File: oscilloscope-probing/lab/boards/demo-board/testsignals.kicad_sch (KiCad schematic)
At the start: 1 part, among them U4 XC7A35T-2FGG484I

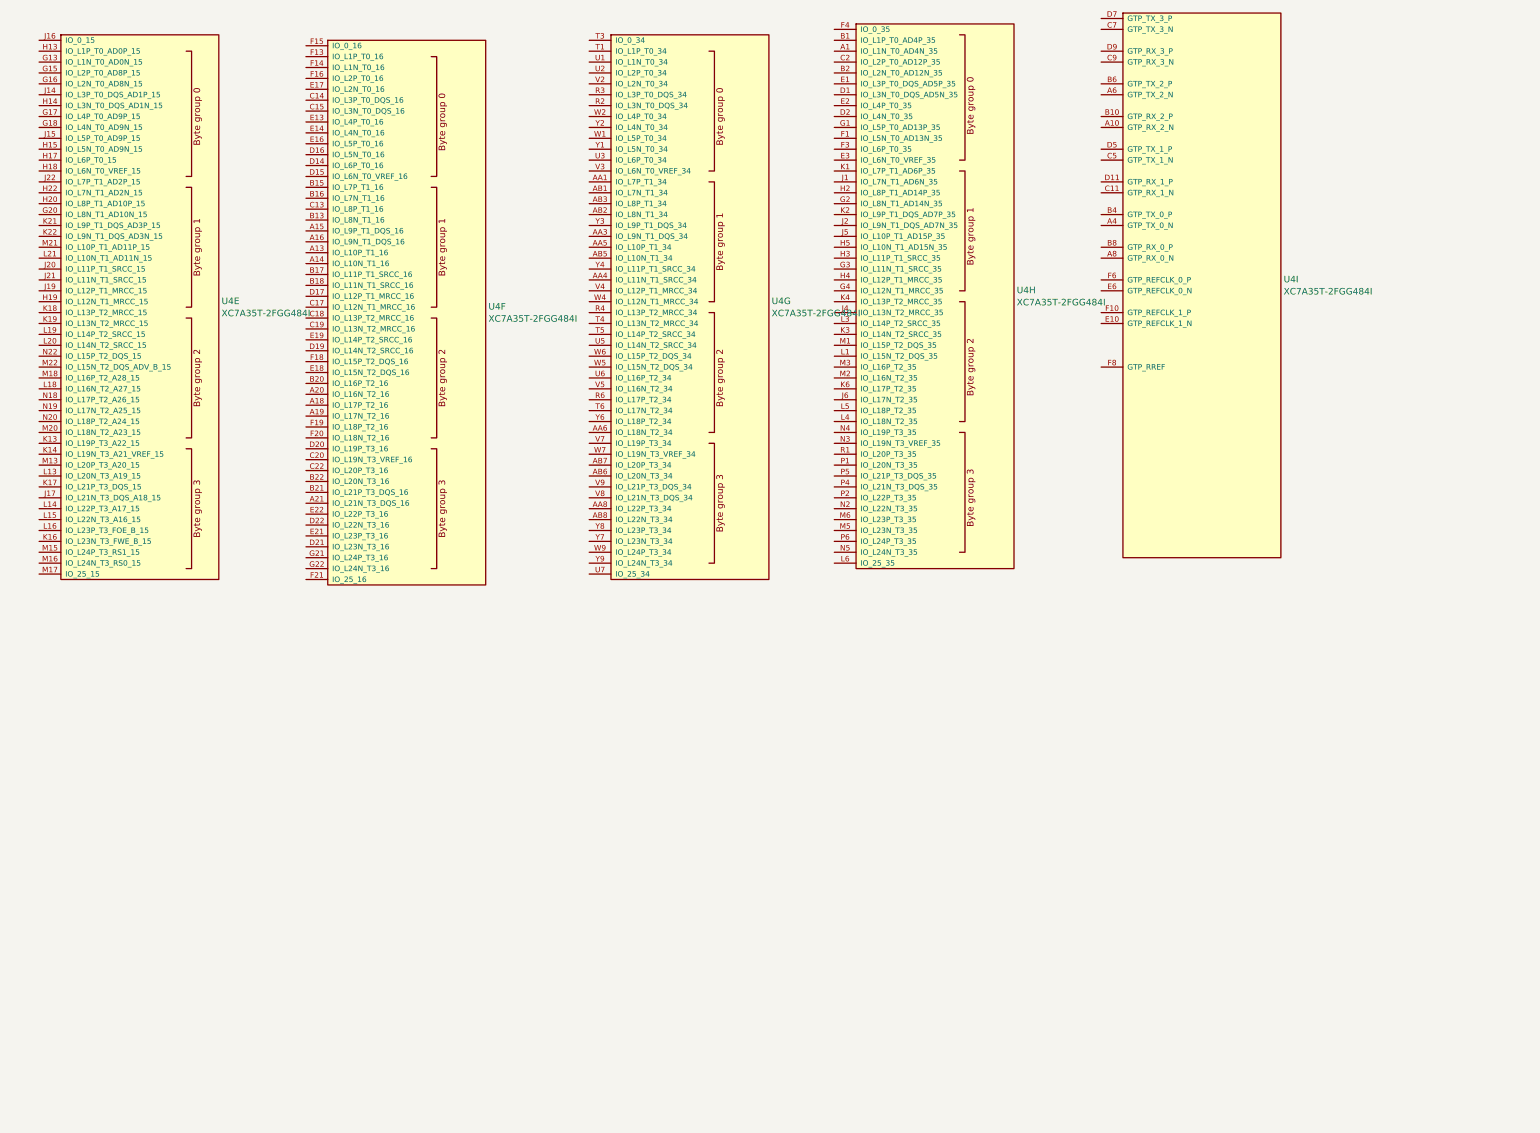
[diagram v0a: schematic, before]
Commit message: Finished initial demo board schematic
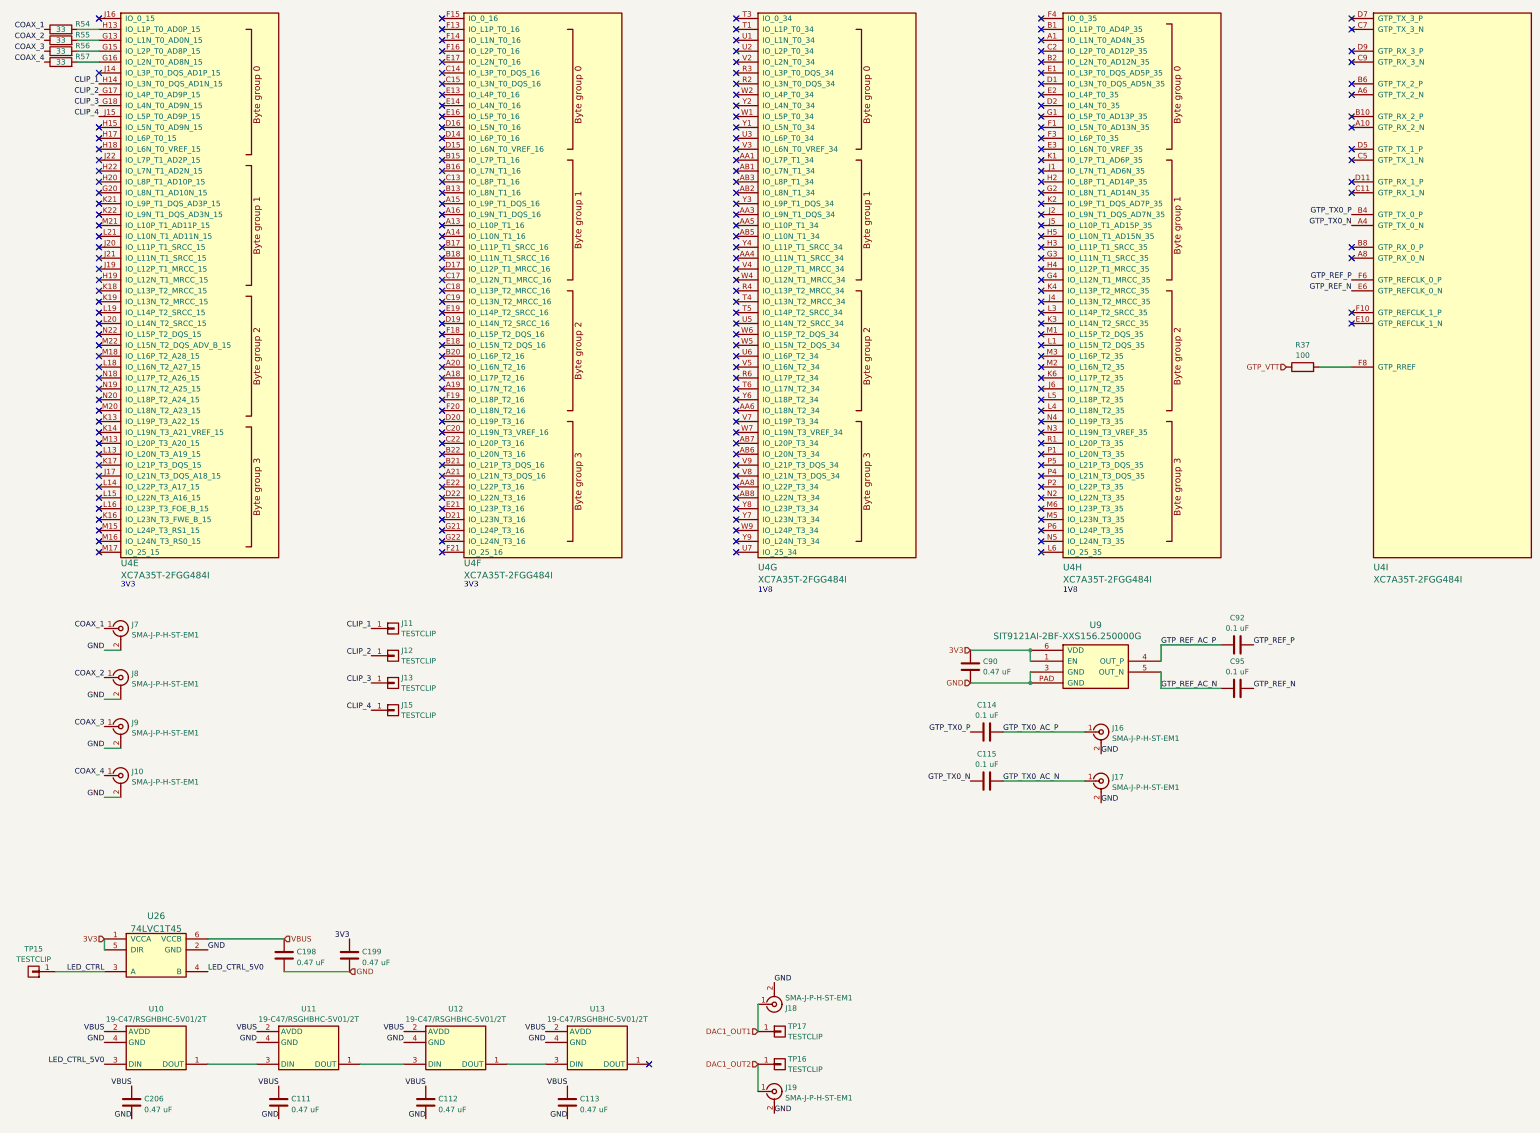
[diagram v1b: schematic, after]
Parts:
- added C111, C112, C113, C198, C199, C206, C90: 0.47 uF, azonenberg_pcb:EIA_0402_CAP_NOSILK, symbol device:C
- added C114, C115, C92, C95: 0.1 uF, azonenberg_pcb:EIA_0402_CAP_NOSILK, symbol device:C
- added J10, J16, J17, J18, J19, J7, J8, J9: SMA-J-P-H-ST-EM1, symbol conn:CONN_COAXIAL
- added J11, J12, J13, J15, TP15, TP16, TP17: TESTCLIP, symbol conn:CONN_01X01
- added R37: 100, azonenberg_pcb:EIA_0402_RES_NOSILK, symbol device:R
- added R54, R55, R56, R57: 33, symbol device:R
- added U10, U11, U12, U13: 19-C47/RSGHBHC-5V01/2T, symbol special-azonenberg:19-C47_RSGHBHC-5V01_2T
- added U26: 74LVC1T45, azonenberg_pcb:DFN_6_0.5MM_1.6x1.6MM_TI_DPK, symbol special-azonenberg:74AVC1T45
- added U9: SIT9121AI-2BF-XXS156.250000G, azonenberg_pcb:OSCILLATOR_LVDS_3.2x2.5, symbol osc-azonenberg:OSC_LVDS
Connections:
- net GTP_TX0_N: now reaches U4.A4 (GTP_TX_0_N)
- net GTP_TX0_N: now also C115.1
- net GTP_TX0_P: now reaches U4.B4 (GTP_TX_0_P)
- net GTP_TX0_P: now also C114.1
- net GTP_REF_N: now reaches U4.E6 (GTP_REFCLK_0_N)
- net GTP_REF_N: now also C95.2
- net GTP_REF_P: now reaches U4.F6 (GTP_REFCLK_0_P)
- net GTP_REF_P: now also C92.2
- net at U4.F8 (GTP_RREF): now also R37.2
- net at U4.G13 (IO_L1N_T0_AD0N_15): now also R55.2
- net at U4.G15 (IO_L2P_T0_AD8P_15): now also R56.2
- net at U4.G16 (IO_L2N_T0_AD8N_15): now also R57.2
- net CLIP_2: now reaches U4.G17 (IO_L4P_T0_AD9P_15)
- net CLIP_2: now also J12.1 (P1)
- net CLIP_3: now reaches U4.G18 (IO_L4N_T0_AD9N_15)
- net CLIP_3: now also J13.1 (P1)
- net at U4.H13 (IO_L1P_T0_AD0P_15): now also R54.2
- net CLIP_1: now reaches U4.H14 (IO_L3N_T0_DQS_AD1N_15)
- net CLIP_1: now also J11.1 (P1)
- net CLIP_4: now reaches U4.J15 (IO_L5P_T0_AD9P_15)
- net CLIP_4: now also J15.1 (P1)
- new net: U11.1 (DOUT), U12.3 (DIN)
- new net: U10.1 (DOUT), U11.3 (DIN)
- new net: U12.1 (DOUT), U13.3 (DIN)
- new net 3V3: C199.1, C90.1, U26.1 (VCCA), U26.5 (DIR), U9.1 (EN), U9.6 (VDD)
- new net COAX_1: J7.1 (In), R54.1
- new net COAX_2: J8.1 (In), R55.1
- new net COAX_3: J9.1 (In), R56.1
- new net COAX_4: J10.1 (In), R57.1
- new net DAC1_OUT1: J18.1 (In), TP17.1 (P1)
- new net DAC1_OUT2: J19.1 (In), TP16.1 (P1)
- new net GND: C111.2, C112.2, C113.2, C198.2, C199.2, C206.2, C90.2, J10.2 (Ext), J16.2 (Ext), J17.2 (Ext), J18.2 (Ext), J19.2 (Ext), J7.2 (Ext), J8.2 (Ext), J9.2 (Ext), U10.4 (GND), U11.4 (GND), U12.4 (GND), U13.4 (GND), U26.2 (GND), U9.3 (GND), U9.PAD (GND)
- new net GTP_REF_AC_N: C95.1, U9.5 (OUT_N)
- new net GTP_REF_AC_P: C92.1, U9.4 (OUT_P)
- new net GTP_TX0_AC_N: C115.2, J17.1 (In)
- new net GTP_TX0_AC_P: C114.2, J16.1 (In)
- new net GTP_VTT: R37.1
- new net LED_CTRL: TP15.1 (P1), U26.3 (A)
- new net LED_CTRL_5V0: U10.3 (DIN), U26.4 (B)
- new net VBUS: C111.1, C112.1, C113.1, C198.1, C206.1, U10.2 (AVDD), U11.2 (AVDD), U12.2 (AVDD), U13.2 (AVDD), U26.6 (VCCB)
- no-connect marks 0 -> 209
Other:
- note added: "1V8"
- note added: "3V3"
- moved on the sheet: U4E, U4F, U4G, U4H, U4I

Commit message: Continued initial schematic, assigned footprints
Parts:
- J10, J16, J17, J18, J19, J7, J8, J9: footprint (none) -> azonenberg_pcb:CONN_SMA_EDGE_SAMTEC_SMA_J_P_H_ST_EM1
- J11, J12, J13, J15, TP15, TP16, TP17: footprint (none) -> azonenberg_pcb:TESTPOINT_SMT_KEYSTONE_5016
- R54, R55, R56, R57: footprint (none) -> azonenberg_pcb:EIA_0402_RES_NOSILK
- U10, U11, U12, U13: footprint (none) -> azonenberg_pcb:LED_EVERLIGHT_19-C47_RSGHBHC-5V01_2T
- U4: footprint (none) -> azonenberg_pcb:BGA_484_22x22_FULLARRAY_1MM
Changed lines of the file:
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@@
 			)
 		)
-		(property "Footprint" ""
+		(property "Footprint" "azonenberg_pcb:CONN_SMA_EDGE_SAMTEC_SMA_J_P_H_ST_EM1"
 			(at 276.86 198.12 0)
 			(effects
@@
 			)
 		)
-		(property "Footprint" ""
+		(property "Footprint" "azonenberg_pcb:TESTPOINT_SMT_KEYSTONE_5016"
 			(at 111.76 162.56 0)
 			(effects
@@
 			)
 		)
-		(property "Footprint" ""
+		(property "Footprint" "azonenberg_pcb:CONN_SMA_EDGE_SAMTEC_SMA_J_P_H_ST_EM1"
 			(at 48.26 173.99 0)
 			(effects
@@
 			)
 		)
-		(property "Footprint" ""
+		(property "Footprint" "azonenberg_pcb:TESTPOINT_SMT_KEYSTONE_5016"
 			(at 111.76 175.26 0)
 			(effects
@@
 			)
 		)
-		(property "Footprint" ""
+		(property "Footprint" "azonenberg_pcb:CONN_SMA_EDGE_SAMTEC_SMA_J_P_H_ST_EM1"
 			(at 48.26 162.56 0)
 			(effects
@@
 			)
 		)
-		(property "Footprint" ""
+		(property "Footprint" "azonenberg_pcb:TESTPOINT_SMT_KEYSTONE_5016"
 			(at 111.76 168.91 0)
 			(effects
@@
 			)
 		)
-		(property "Footprint" ""
+		(property "Footprint" "azonenberg_pcb:TESTPOINT_SMT_KEYSTONE_5016"
 			(at 111.76 181.61 0)
 			(effects
@@
 			)
 		)
-		(property "Footprint" ""
+		(property "Footprint" "azonenberg_pcb:TESTPOINT_SMT_KEYSTONE_5016"
 			(at 201.93 264.16 0)
 			(effects
@@
 			)
 		)
-		(property "Footprint" ""
+		(property "Footprint" "azonenberg_pcb:BGA_484_22x22_FULLARRAY_1MM"
 			(at 340.36 152.4 0)
 			(effects
@@
 					(size 1.524 1.524)
 				)
+				(hide yes)
 			)
 		)
@@
 			)
 		)
-		(property "Footprint" ""
+		(property "Footprint" "azonenberg_pcb:EIA_0402_RES_NOSILK"
 			(at 34.29 24.638 90)
 			(effects
@@
 			)
 		)
-		(property "Footprint" ""
+		(property "Footprint" "azonenberg_pcb:EIA_0402_RES_NOSILK"
 			(at 34.29 29.718 90)
 			(effects
@@
 			)
 		)
-		(property "Footprint" ""
+		(property "Footprint" "azonenberg_pcb:CONN_SMA_EDGE_SAMTEC_SMA_J_P_H_ST_EM1"
 			(at 276.86 186.69 0)
 			(effects
@@
 			)
 		)
-		(property "Footprint" ""
+		(property "Footprint" "azonenberg_pcb:TESTPOINT_SMT_KEYSTONE_5016"
 			(at 27.94 242.57 0)
 			(effects
@@
 			)
 		)
-		(property "Footprint" ""
+		(property "Footprint" "azonenberg_pcb:TESTPOINT_SMT_KEYSTONE_5016"
 			(at 201.93 256.54 0)
 			(effects
@@
 			)
 		)
-		(property "Footprint" ""
+		(property "Footprint" "azonenberg_pcb:BGA_484_22x22_FULLARRAY_1MM"
 			(at 48.26 152.4 0)
 			(effects
@@
 					(size 1.524 1.524)
 				)
+				(hide yes)
 			)
 		)
@@
 			)
 		)
-		(property "Footprint" ""
+		(property "Footprint" "azonenberg_pcb:EIA_0402_RES_NOSILK"
 			(at 34.29 27.178 90)
 			(effects
@@
 			)
 		)
-		(property "Footprint" ""
+		(property "Footprint" "azonenberg_pcb:CONN_SMA_EDGE_SAMTEC_SMA_J_P_H_ST_EM1"
 			(at 48.26 185.42 0)
 			(effects
@@
 			)
 		)
-		(property "Footprint" ""
+		(property "Footprint" "azonenberg_pcb:CONN_SMA_EDGE_SAMTEC_SMA_J_P_H_ST_EM1"
 			(at 200.66 270.51 0)
 			(effects
@@
 			)
 		)
-		(property "Footprint" ""
+		(property "Footprint" "azonenberg_pcb:CONN_SMA_EDGE_SAMTEC_SMA_J_P_H_ST_EM1"
 			(at 200.66 250.19 0)
 			(effects
@@
 			)
 		)
-		(property "Footprint" ""
+		(property "Footprint" "azonenberg_pcb:CONN_SMA_EDGE_SAMTEC_SMA_J_P_H_ST_EM1"
 			(at 48.26 196.85 0)
 			(effects
@@
 			)
 		)
-		(property "Footprint" ""
+		(property "Footprint" "azonenberg_pcb:LED_EVERLIGHT_19-C47_RSGHBHC-5V01_2T"
 			(at 85.09 265.43 0)
 			(effects
@@
 			)
 		)
-		(property "Footprint" ""
+		(property "Footprint" "azonenberg_pcb:BGA_484_22x22_FULLARRAY_1MM"
 			(at 128.27 152.4 0)
 			(effects
@@
 					(size 1.524 1.524)
 				)
+				(hide yes)
 			)
 		)
@@
 			)
 		)
-		(property "Footprint" ""
+		(property "Footprint" "azonenberg_pcb:BGA_484_22x22_FULLARRAY_1MM"
 			(at 267.97 152.4 0)
 			(effects
@@
 					(size 1.524 1.524)
 				)
+				(hide yes)
 			)
 		)
@@
 			)
 		)
-		(property "Footprint" ""
+		(property "Footprint" "azonenberg_pcb:LED_EVERLIGHT_19-C47_RSGHBHC-5V01_2T"
 			(at 119.38 265.43 0)
 			(effects
@@
 			)
 		)
-		(property "Footprint" ""
+		(property "Footprint" "azonenberg_pcb:LED_EVERLIGHT_19-C47_RSGHBHC-5V01_2T"
 			(at 49.53 265.43 0)
 			(effects
@@
 			)
 		)
-		(property "Footprint" ""
+		(property "Footprint" "azonenberg_pcb:EIA_0402_RES_NOSILK"
 			(at 34.29 32.258 90)
 			(effects
@@
 			)
 		)
-		(property "Footprint" ""
+		(property "Footprint" "azonenberg_pcb:LED_EVERLIGHT_19-C47_RSGHBHC-5V01_2T"
 			(at 152.4 265.43 0)
 			(effects
@@
 			)
 		)
-		(property "Footprint" ""
+		(property "Footprint" "azonenberg_pcb:BGA_484_22x22_FULLARRAY_1MM"
 			(at 196.85 152.4 0)
 			(effects
@@
 					(size 1.524 1.524)
 				)
+				(hide yes)
 			)
 		)

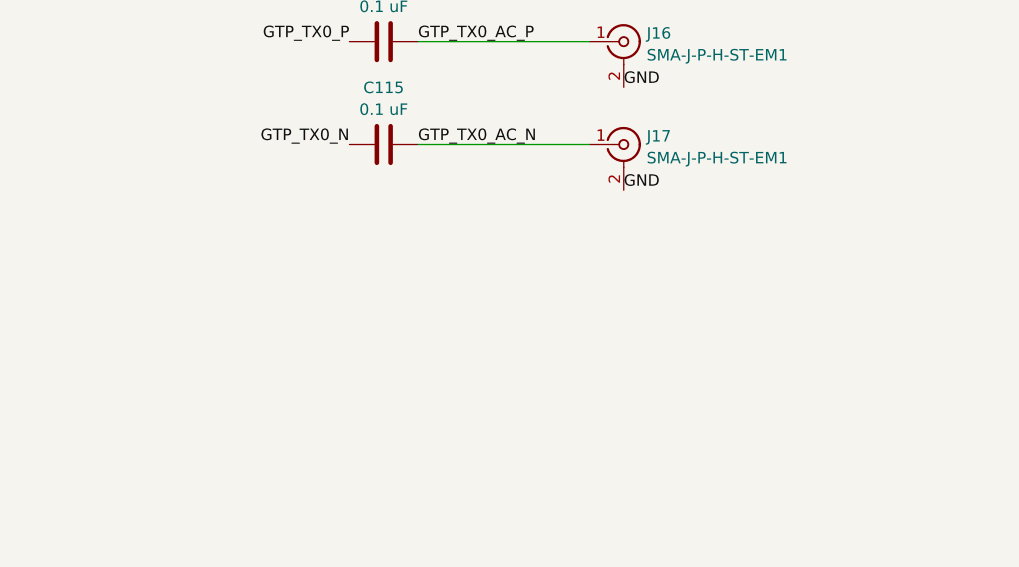
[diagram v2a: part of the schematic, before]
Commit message: Continued demo board layout
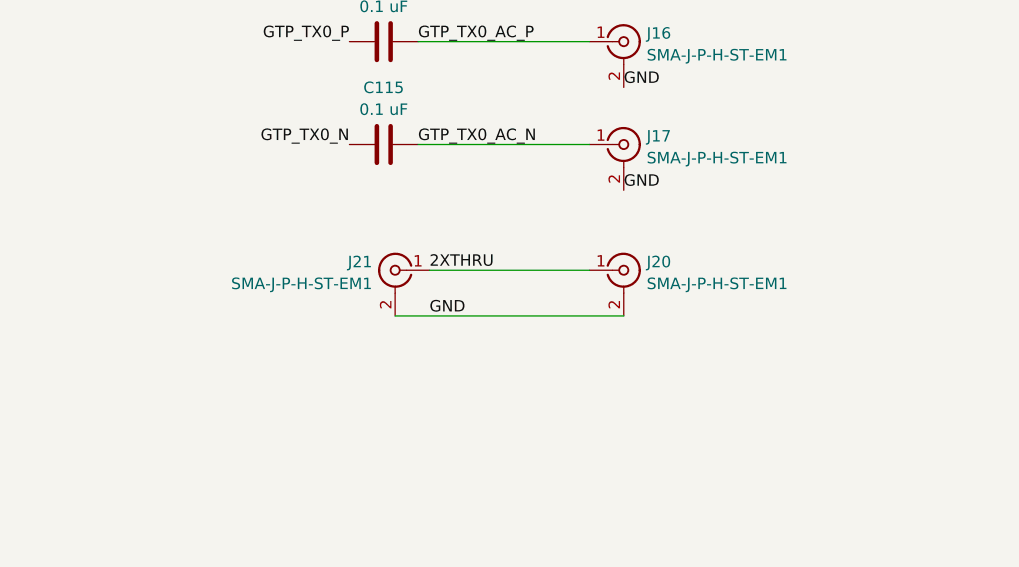
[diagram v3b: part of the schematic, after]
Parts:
- added J20, J21: SMA-J-P-H-ST-EM1, azonenberg_pcb:CONN_SMA_EDGE_SAMTEC_SMA_J_P_H_ST_EM1, symbol conn:CONN_COAXIAL
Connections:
- net GND: now also J20.2 (Ext), J21.2 (Ext)
- new net 2XTHRU: J20.1 (In), J21.1 (In)
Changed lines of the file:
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@@
 	(wire
 		(pts
+			(xy 255.27 212.09) (xy 273.05 212.09)
+		)
+		(stroke
+			(width 0)
+			(type default)
+		)
+	)
+	(wire
+		(pts
+			(xy 251.46 217.17) (xy 276.86 217.17)
+		)
+		(stroke
+			(width 0)
+			(type default)
+		)
+	)
+	(wire
+		(pts
 			(xy 304.8 166.37) (xy 290.83 166.37)
 		)
@@
 		)
 	)
+	(label "GND"
+		(at 255.27 217.17 0)
+		(effects
+			(font
+				(size 1.27 1.27)
+			)
+			(justify left bottom)
+		)
+	)
 	(label "GTP_TX0_P"
 		(at 335.28 66.04 180)
@@
 		)
 	)
+	(label "2XTHRU"
+		(at 255.27 212.09 0)
+		(effects
+			(font
+				(size 1.27 1.27)
+			)
+			(justify left bottom)
+		)
+	)
 	(label "GND"
 		(at 44.45 201.93 180)
@@
 	(symbol
 		(lib_id "conn:CONN_COAXIAL")
+		(at 251.46 212.09 0)
+		(mirror y)
+		(unit 1)
+		(exclude_from_sim no)
+		(in_bom yes)
+		(on_board yes)
+		(dnp no)
+		(property "Reference" "J21"
+			(at 248.92 211.171 0)
+			(effects
+				(font
+					(size 1.27 1.27)
+				)
+				(justify left)
+			)
+		)
+		(property "Value" "SMA-J-P-H-ST-EM1"
+			(at 248.92 213.5953 0)
+			(effects
+				(font
+					(size 1.27 1.27)
+				)
+				(justify left)
+			)
+		)
+		(property "Footprint" "azonenberg_pcb:CONN_SMA_EDGE_SAMTEC_SMA_J_P_H_ST_EM1"
+			(at 251.46 212.09 0)
+			(effects
+				(font
+					(size 1.27 1.27)
+				)
+				(hide yes)
+			)
+		)
+		(property "Datasheet" ""
+			(at 251.46 212.09 0)
+			(effects
+				(font
+					(size 1.27 1.27)
+				)
+				(hide yes)
+			)
+		)
+		(property "Description" "coaxial connector (BNC, SMA, SMB, SMC, Cinch/RCA, ...)"
+			(at 251.46 212.09 0)
+			(effects
+				(font
+					(size 1.27 1.27)
+				)
+				(hide yes)
+			)
+		)
+		(pin "2"
+		)
+		(pin "1"
+		)
+		(instances
+			(project "demo-board"
+				(path "/aa2d82c6-7ba7-4266-9b47-ed3339e6c556/a5c6d6a0-0eb9-4128-8a96-febfa5d4e510"
+					(reference "J21")
+					(unit 1)
+				)
+			)
+		)
+	)
+	(symbol
+		(lib_id "conn:CONN_COAXIAL")
 		(at 48.26 173.99 0)
 		(unit 1)
@@
 				)
 			)
+		)
+	)
+	(symbol
+		(lib_id "conn:CONN_COAXIAL")
+		(at 276.86 212.09 0)
+		(unit 1)
+		(exclude_from_sim no)
+		(in_bom yes)
+		(on_board yes)
+		(dnp no)
+		(fields_autoplaced yes)
+		(property "Reference" "J20"
+			(at 279.4 211.171 0)
+			(effects
+				(font
+					(size 1.27 1.27)
+				)
+				(justify left)
+			)
+		)
+		(property "Value" "SMA-J-P-H-ST-EM1"
+			(at 279.4 213.5953 0)
+			(effects
+				(font
+					(size 1.27 1.27)
+				)
+				(justify left)
+			)
+		)
+		(property "Footprint" "azonenberg_pcb:CONN_SMA_EDGE_SAMTEC_SMA_J_P_H_ST_EM1"
+			(at 276.86 212.09 0)
+			(effects
+				(font
+					(size 1.27 1.27)
+				)
+				(hide yes)
+			)
+		)
+		(property "Datasheet" ""
+			(at 276.86 212.09 0)
+			(effects
+				(font
+					(size 1.27 1.27)
+				)
+				(hide yes)
+			)
+		)
+		(property "Description" "coaxial connector (BNC, SMA, SMB, SMC, Cinch/RCA, ...)"
+			(at 276.86 212.09 0)
+			(effects
+				(font
+					(size 1.27 1.27)
+				)
+				(hide yes)
+			)
+		)
+		(pin "2"
+		)
+		(pin "1"
+		)
+		(instances
+			(project "demo-board"
+				(path "/aa2d82c6-7ba7-4266-9b47-ed3339e6c556/a5c6d6a0-0eb9-4128-8a96-febfa5d4e510"
+					(reference "J20")
+					(unit 1)
+				)
+			)
